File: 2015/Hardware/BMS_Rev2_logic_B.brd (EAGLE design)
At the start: 45.4 x 57.3 mm, 38 parts, among them Q9 MOSFET-NCHANNEL2N7002PW

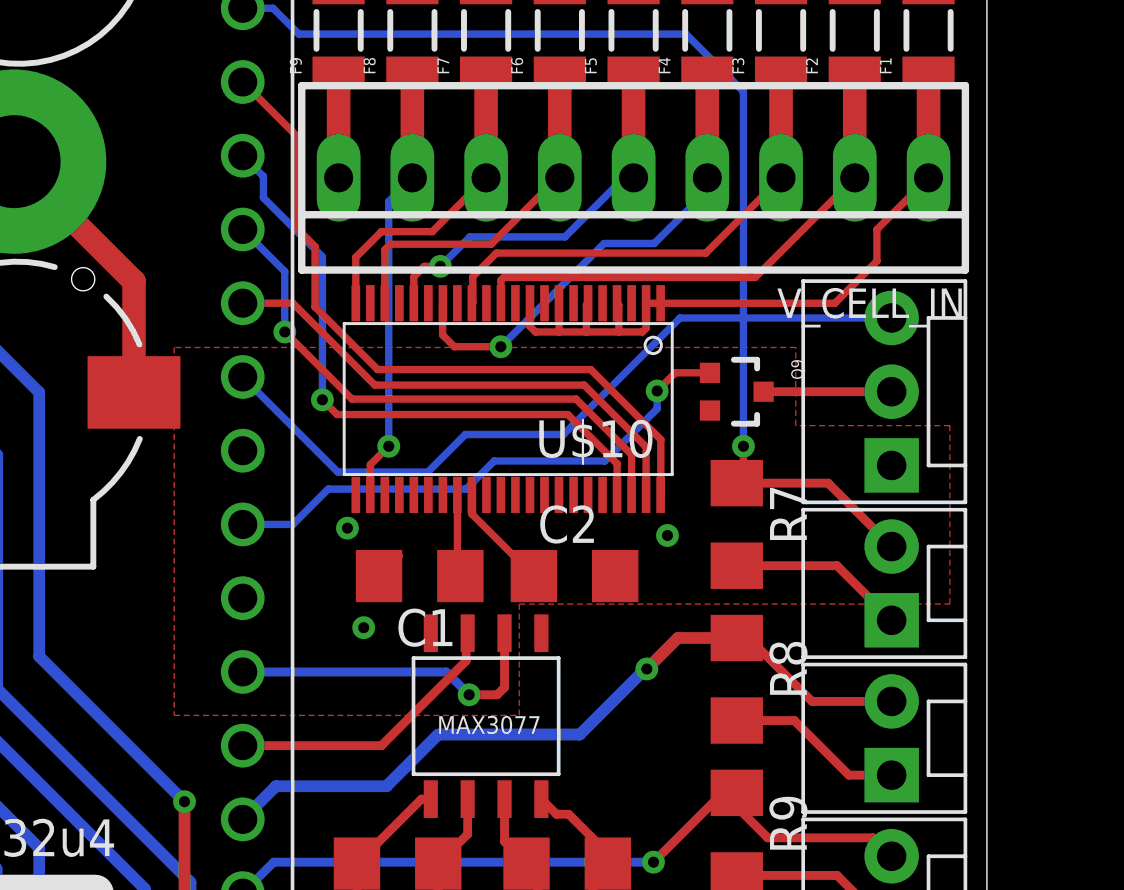
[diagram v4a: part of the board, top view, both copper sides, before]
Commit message: Cleaned up traces, but routing still needed. Clearance and poor traces
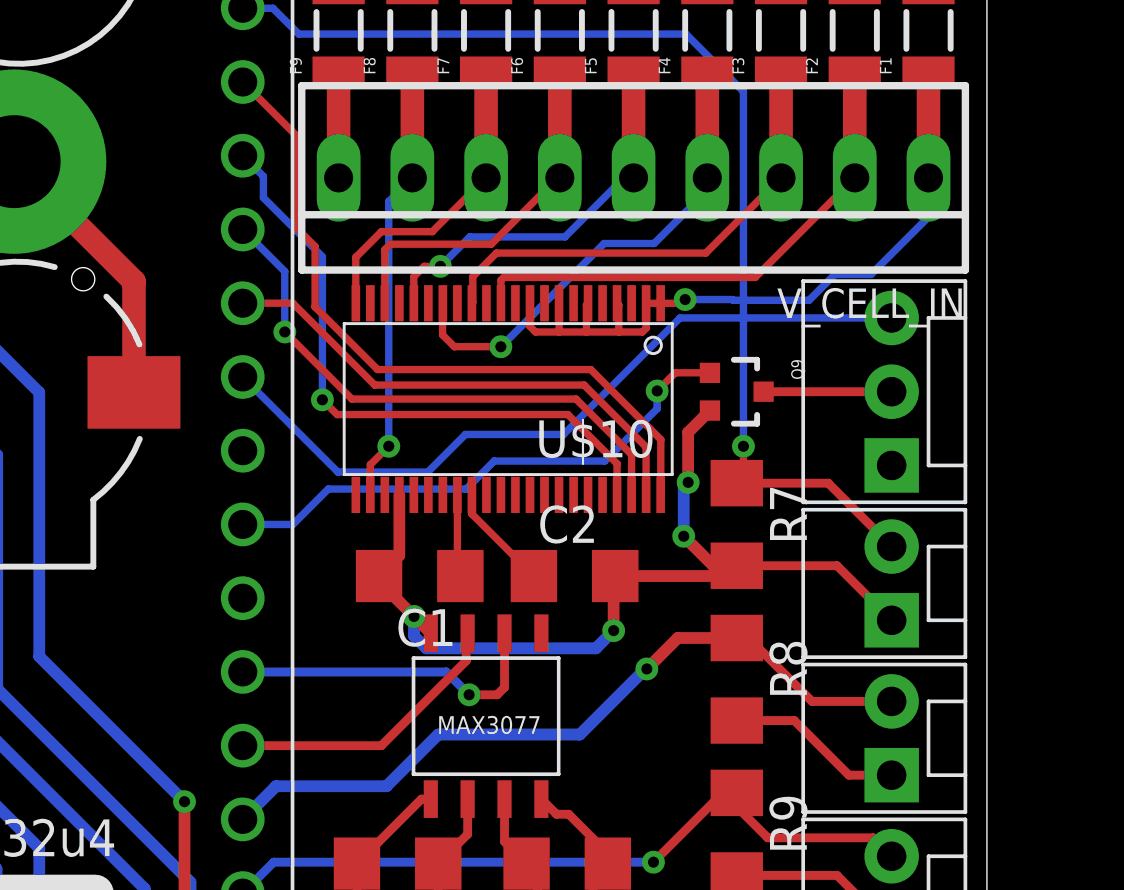
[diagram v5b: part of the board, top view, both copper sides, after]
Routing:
- net GND: track 45.4 -> 70.7 mm, vias 0 -> 4
- net N$41: track 24.6 -> 24.8 mm, vias 0 -> 1
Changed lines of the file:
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@@
 <wire x1="15.3242" y1="1.1176" x2="15.3242" y2="10.803" width="0.6096" layer="1"/>
 <wire x1="15.3242" y1="10.803" x2="15.3416" y2="10.8204" width="0.6096" layer="1"/>
-<wire x1="30.099" y1="23.1775" x2="42.164" y2="28.956" width="0" layer="19" extent="1-1"/>
 </signal>
 <signal name="GND">
@@
 <wire x1="23.114" y1="38.862" x2="23.114" y2="42.542" width="0.8128" layer="1"/>
 <wire x1="25.206" y1="25.844" x2="24.508" y2="25.146" width="0.254" layer="1"/>
-<wire x1="24.508" y1="25.146" x2="24.508" y2="24.9585" width="0.254" layer="1"/>
 <wire x1="36.474" y1="25.146" x2="36.83" y2="25.502" width="0.254" layer="1"/>
 <contactref element="S1" pad="P1"/>
@@
 <wire x1="16.0904" y1="47.2948" x2="18.5796" y2="49.784" width="0.8128" layer="1"/>
 <wire x1="18.5796" y1="49.784" x2="19.812" y2="49.784" width="0.8128" layer="1"/>
-<polygon width="0.4064" layer="1">
-<vertex x="17.4498" y="28.0924"/>
-<vertex x="17.4498" y="20.3454"/>
-<vertex x="29.337" y="20.3454"/>
-<vertex x="29.337" y="24.1808"/>
-<vertex x="32.0802" y="24.1808"/>
-<vertex x="44.1706" y="24.1808"/>
-<vertex x="44.1706" y="30.3276"/>
-<vertex x="38.862" y="30.3276"/>
-<vertex x="38.862" y="33.02"/>
-<vertex x="17.4498" y="33.02"/>
-</polygon>
-<wire x1="25.206" y1="25.844" x2="25.206" y2="27.942" width="0" layer="19" extent="1-1"/>
+<wire x1="26.289" y1="23.1775" x2="25.71115" y2="23.75535" width="0.4064" layer="1"/>
+<wire x1="24.508" y1="24.9585" x2="24.508" y2="25.146" width="0.4064" layer="1"/>
+<wire x1="25.206" y1="25.844" x2="25.206" y2="27.942" width="0.4064" layer="1"/>
+<wire x1="32.642" y1="25.146" x2="36.474" y2="25.146" width="0.4064" layer="1"/>
+<wire x1="32.642" y1="25.146" x2="32.5882" y2="25.0922" width="0.4064" layer="1"/>
+<wire x1="32.5882" y1="25.0922" x2="32.5882" y2="23.2664" width="0.4064" layer="1"/>
+<via x="32.5882" y="23.2664" extent="1-16" drill="0.381"/>
+<wire x1="32.5882" y1="23.2664" x2="31.9786" y2="22.6568" width="0.4064" layer="16"/>
+<wire x1="31.9786" y1="22.6568" x2="26.1366" y2="22.6568" width="0.4064" layer="16"/>
+<wire x1="26.1366" y1="22.6568" x2="25.71115" y2="23.08225" width="0.4064" layer="16"/>
+<wire x1="25.71115" y1="23.08225" x2="25.71115" y2="23.75535" width="0.4064" layer="16"/>
+<via x="25.71115" y="23.75535" extent="1-16" drill="0.381"/>
+<wire x1="25.71115" y1="23.75535" x2="24.508" y2="24.9585" width="0.4064" layer="1"/>
+<wire x1="35.905" y1="30.846" x2="35.1536" y2="30.0946" width="0.4064" layer="1"/>
+<wire x1="35.1536" y1="30.0946" x2="35.1536" y2="28.3718" width="0.4064" layer="1"/>
+<via x="35.1536" y="28.3718" extent="1-16" drill="0.381"/>
+<wire x1="35.1536" y1="28.3718" x2="35.0012" y2="28.2194" width="0.4064" layer="16"/>
+<wire x1="35.0012" y1="28.2194" x2="35.0012" y2="26.5176" width="0.4064" layer="16"/>
+<via x="35.0012" y="26.5176" extent="1-16" drill="0.381"/>
+<wire x1="35.0012" y1="26.5176" x2="36.0168" y2="25.502" width="0.4064" layer="1"/>
+<wire x1="36.0168" y1="25.502" x2="36.83" y2="25.502" width="0.4064" layer="1"/>
 </signal>
 <signal name="GATE">
@@
 <contactref element="F1" pad="1"/>
 <wire x1="43.434" y1="38.862" x2="43.434" y2="42.542" width="0.8128" layer="1"/>
-<wire x1="34.206" y1="34.542" x2="40.2062" y2="34.542" width="0.254" layer="1"/>
-<wire x1="40.2062" y1="34.542" x2="41.656" y2="35.9918" width="0.254" layer="1"/>
-<wire x1="41.656" y1="35.9918" x2="41.656" y2="37.084" width="0.254" layer="1"/>
-<wire x1="41.656" y1="37.084" x2="43.434" y2="38.862" width="0.254" layer="1"/>
 <wire x1="33.706" y1="34.542" x2="34.206" y2="34.542" width="0.254" layer="1"/>
 <wire x1="33.706" y1="34.542" x2="33.706" y2="33.6806" width="0.254" layer="1"/>
@@
 <wire x1="32.706" y1="34.542" x2="32.766" y2="34.482" width="0.254" layer="1"/>
 <wire x1="32.766" y1="34.482" x2="32.766" y2="33.5534" width="0.254" layer="1"/>
+<wire x1="43.434" y1="38.862" x2="43.434" y2="37.5158" width="0.254" layer="16"/>
+<wire x1="43.434" y1="37.5158" x2="41.4528" y2="35.5346" width="0.254" layer="16"/>
+<wire x1="41.4528" y1="35.5346" x2="40.2082" y2="35.5346" width="0.254" layer="16"/>
+<wire x1="40.2082" y1="35.5346" x2="39.3192" y2="34.6456" width="0.254" layer="16"/>
+<wire x1="39.3192" y1="34.6456" x2="36.703" y2="34.6456" width="0.254" layer="16"/>
+<wire x1="36.703" y1="34.6456" x2="36.6776" y2="34.671" width="0.254" layer="16"/>
+<wire x1="36.6776" y1="34.671" x2="35.052" y2="34.671" width="0.254" layer="16"/>
+<via x="35.052" y="34.671" extent="1-16" drill="0.381"/>
+<wire x1="35.052" y1="34.671" x2="34.923" y2="34.542" width="0.254" layer="1"/>
+<wire x1="34.923" y1="34.542" x2="34.206" y2="34.542" width="0.254" layer="1"/>
 </signal>
 <signal name="N$42">
@@
 <wire x1="42.164" y1="31.496" x2="37.755" y2="31.496" width="0.3048" layer="1"/>
 </signal>
-<signal name="N$8">
-<via x="23.4188" y="26.797" extent="1-16" drill="0.381"/>
-</signal>
-<signal name="N$19">
-<via x="23.9776" y="23.368" extent="1-16" drill="0.381"/>
-</signal>
-<signal name="N$20">
-<via x="34.4424" y="26.543" extent="1-16" drill="0.381"/>
-</signal>
 <signal name="LCD_TX">

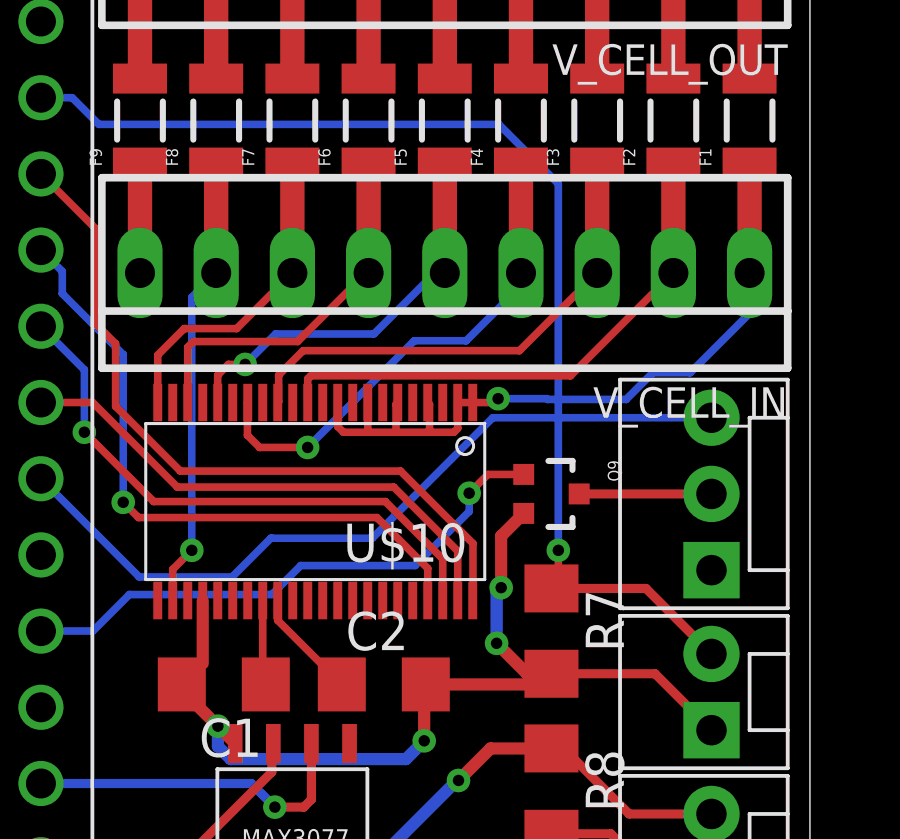
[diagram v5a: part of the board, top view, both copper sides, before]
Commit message: Still fixing DRC errors
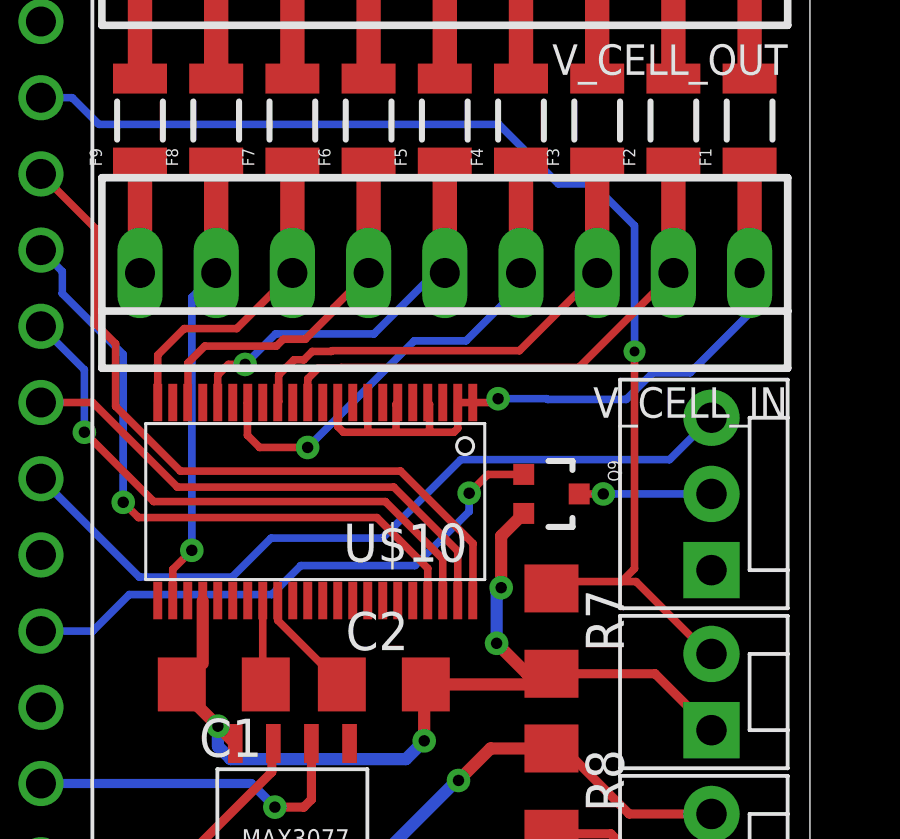
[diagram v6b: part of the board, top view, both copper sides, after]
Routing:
- net SW_INSTALLED: track 38.3 -> 40.3 mm
- net N$5: vias 0 -> 1
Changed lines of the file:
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@@
 <?xml version="1.0" encoding="utf-8"?>
 <!DOCTYPE eagle SYSTEM "eagle.dtd">
-<eagle version="6.5.0">
+<eagle version="6.6.0">
 <drawing>
 <settings>
@@
 </class>
 </classes>
-<designrules name="default">
+<designrules name="default *">
 <description language="de">&lt;b&gt;EAGLE Design Rules&lt;/b&gt;
 &lt;p&gt;
@@
 <param name="mdPadVia" value="8mil"/>
 <param name="mdViaVia" value="8mil"/>
-<param name="mdSmdPad" value="8mil"/>
-<param name="mdSmdVia" value="8mil"/>
-<param name="mdSmdSmd" value="8mil"/>
+<param name="mdSmdPad" value="0mil"/>
+<param name="mdSmdVia" value="0mil"/>
+<param name="mdSmdSmd" value="0mil"/>
 <param name="mdViaViaSameLayer" value="8mil"/>
 <param name="mnLayersViaInSmd" value="2"/>
@@
 <wire x1="40.894" y1="38.862" x2="40.894" y2="42.542" width="0.8128" layer="1"/>
 <wire x1="28.706" y1="34.542" x2="28.706" y2="35.3354" width="0.254" layer="1"/>
-<wire x1="28.706" y1="35.3354" x2="28.8036" y2="35.433" width="0.254" layer="1"/>
-<wire x1="28.8036" y1="35.433" x2="37.465" y2="35.433" width="0.254" layer="1"/>
-<wire x1="37.465" y1="35.433" x2="40.894" y2="38.862" width="0.254" layer="1"/>
+<wire x1="37.7444" y1="35.7124" x2="40.894" y2="38.862" width="0.254" layer="1"/>
+<wire x1="28.706" y1="35.3354" x2="29.0576" y2="35.687" width="0.254" layer="1"/>
+<wire x1="29.0576" y1="35.687" x2="29.7942" y2="35.687" width="0.254" layer="1"/>
+<wire x1="29.7942" y1="35.687" x2="29.8196" y2="35.7124" width="0.254" layer="1"/>
+<wire x1="29.8196" y1="35.7124" x2="37.7444" y2="35.7124" width="0.254" layer="1"/>
 </signal>
 <signal name="N$43">
@@
 <wire x1="27.706" y1="34.542" x2="27.7368" y2="34.5728" width="0.254" layer="1"/>
 <wire x1="27.7368" y1="34.5728" x2="27.7368" y2="35.4584" width="0.254" layer="1"/>
-<wire x1="28.5496" y1="36.2712" x2="35.7632" y2="36.2712" width="0.254" layer="1"/>
 <wire x1="35.7632" y1="36.2712" x2="38.354" y2="38.862" width="0.254" layer="1"/>
-<wire x1="27.7368" y1="35.4584" x2="28.5496" y2="36.2712" width="0.254" layer="1"/>
+<wire x1="27.7368" y1="35.4584" x2="28.2448" y2="35.9664" width="0.254" layer="1"/>
+<wire x1="28.2448" y1="35.9664" x2="28.575" y2="35.9664" width="0.254" layer="1"/>
+<wire x1="28.575" y1="35.9664" x2="28.8544" y2="36.2458" width="0.254" layer="1"/>
+<wire x1="28.8544" y1="36.2458" x2="29.4894" y2="36.2458" width="0.254" layer="1"/>
+<wire x1="29.4894" y1="36.2458" x2="29.5148" y2="36.2712" width="0.254" layer="1"/>
+<wire x1="29.5148" y1="36.2712" x2="35.7632" y2="36.2712" width="0.254" layer="1"/>
 </signal>
 <signal name="N$46">
@@
 <contactref element="F6" pad="1"/>
 <wire x1="30.734" y1="38.862" x2="30.734" y2="42.542" width="0.8128" layer="1"/>
-<wire x1="24.706" y1="34.542" x2="24.706" y2="36.39" width="0.254" layer="1"/>
-<wire x1="24.706" y1="36.39" x2="24.892" y2="36.576" width="0.254" layer="1"/>
-<wire x1="24.892" y1="36.576" x2="28.3718" y2="36.576" width="0.254" layer="1"/>
-<wire x1="28.3718" y1="36.576" x2="30.6578" y2="38.862" width="0.254" layer="1"/>
 <wire x1="30.6578" y1="38.862" x2="30.734" y2="38.862" width="0.254" layer="1"/>
+<wire x1="24.706" y1="34.542" x2="24.7142" y2="34.5502" width="0.254" layer="1"/>
+<wire x1="24.7142" y1="34.5502" x2="24.7142" y2="35.8648" width="0.254" layer="1"/>
+<wire x1="24.7142" y1="35.8648" x2="25.273" y2="36.4236" width="0.254" layer="1"/>
+<wire x1="25.273" y1="36.4236" x2="27.6606" y2="36.4236" width="0.254" layer="1"/>
+<wire x1="27.6606" y1="36.4236" x2="27.8892" y2="36.6522" width="0.254" layer="1"/>
+<wire x1="27.8892" y1="36.6522" x2="28.6258" y2="36.6522" width="0.254" layer="1"/>
+<wire x1="28.6258" y1="36.6522" x2="29.5656" y2="37.592" width="0.254" layer="1"/>
+<wire x1="29.5656" y1="37.592" x2="29.5656" y2="37.6936" width="0.254" layer="1"/>
+<wire x1="29.5656" y1="37.6936" x2="30.734" y2="38.862" width="0.254" layer="1"/>
 </signal>
 <signal name="N$47">
@@
 <contactref element="R7" pad="1"/>
 <contactref element="U$3" pad="13"/>
-<wire x1="42.164" y1="26.162" x2="39.98" y2="28.346" width="0.3048" layer="1"/>
-<wire x1="39.98" y1="28.346" x2="36.83" y2="28.346" width="0.3048" layer="1"/>
 <wire x1="19.812" y1="44.704" x2="20.8534" y2="44.704" width="0.254" layer="16"/>
 <wire x1="20.8534" y1="44.704" x2="21.7424" y2="43.815" width="0.254" layer="16"/>
 <wire x1="21.7424" y1="43.815" x2="35.0774" y2="43.815" width="0.254" layer="16"/>
 <wire x1="35.0774" y1="43.815" x2="37.0586" y2="41.8338" width="0.254" layer="16"/>
-<wire x1="37.0586" y1="41.8338" x2="37.0586" y2="29.6164" width="0.254" layer="16"/>
-<via x="37.0586" y="29.6164" extent="1-16" drill="0.381"/>
-<wire x1="37.0586" y1="29.6164" x2="37.0586" y2="28.5746" width="0.254" layer="1"/>
 <wire x1="37.0586" y1="28.5746" x2="36.83" y2="28.346" width="0.254" layer="1"/>
+<wire x1="37.0586" y1="41.8338" x2="38.2016" y2="41.8338" width="0.254" layer="16"/>
+<wire x1="38.2016" y1="41.8338" x2="39.5986" y2="40.4368" width="0.254" layer="16"/>
+<wire x1="39.5986" y1="40.4368" x2="39.5986" y2="36.2458" width="0.254" layer="16"/>
+<via x="39.5986" y="36.2458" extent="1-16" drill="0.3302"/>
+<wire x1="39.5986" y1="36.2458" x2="39.5986" y2="29.0068" width="0.254" layer="1"/>
+<wire x1="39.5986" y1="29.0068" x2="39.1668" y2="28.575" width="0.254" layer="1"/>
+<wire x1="39.1668" y1="28.575" x2="37.059" y2="28.575" width="0.254" layer="1"/>
+<wire x1="37.059" y1="28.575" x2="36.83" y2="28.346" width="0.254" layer="1"/>
+<wire x1="42.164" y1="26.162" x2="42.0624" y2="26.162" width="0.254" layer="1"/>
+<wire x1="42.0624" y1="26.162" x2="39.6494" y2="28.575" width="0.254" layer="1"/>
+<wire x1="39.6494" y1="28.575" x2="39.1668" y2="28.575" width="0.254" layer="1"/>
 </signal>
 <signal name="SW_LCDWAKE">
@@
 <contactref element="LCD" pad="2"/>
 <contactref element="Q9" pad="3"/>
-<wire x1="42.164" y1="31.496" x2="37.755" y2="31.496" width="0.3048" layer="1"/>
+<wire x1="37.755" y1="31.496" x2="38.5572" y2="31.496" width="0.254" layer="1"/>
+<via x="38.5572" y="31.496" extent="1-16" drill="0.381"/>
+<wire x1="38.5572" y1="31.496" x2="42.164" y2="31.496" width="0.254" layer="16"/>
 </signal>
 <signal name="LCD_TX">
 <contactref element="U$3" pad="8"/>
 <contactref element="LCD" pad="3"/>
-<wire x1="42.164" y1="34.036" x2="34.8742" y2="34.036" width="0.254" layer="16"/>
-<wire x1="34.8742" y1="34.036" x2="30.861" y2="30.0228" width="0.254" layer="16"/>
-<wire x1="30.861" y1="30.0228" x2="27.4828" y2="30.0228" width="0.254" layer="16"/>
+<wire x1="31.1912" y1="30.0228" x2="27.4828" y2="30.0228" width="0.254" layer="16"/>
 <wire x1="27.4828" y1="30.0228" x2="26.1874" y2="28.7274" width="0.254" layer="16"/>
 <wire x1="26.1874" y1="28.7274" x2="23.0886" y2="28.7274" width="0.254" layer="16"/>
 <wire x1="23.0886" y1="28.7274" x2="19.812" y2="32.004" width="0.254" layer="16"/>
+<wire x1="31.1912" y1="30.0228" x2="33.8074" y2="32.639" width="0.254" layer="16"/>
+<wire x1="33.8074" y1="32.639" x2="40.767" y2="32.639" width="0.254" layer="16"/>
+<wire x1="40.767" y1="32.639" x2="42.164" y2="34.036" width="0.254" layer="16"/>
 </signal>
 </signals>
